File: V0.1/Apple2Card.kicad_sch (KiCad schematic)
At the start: 61 parts, among them J1 Conn_01x08_Pin, P2 Conn_02x13_Top_Bottom, Q1 BS170, SW1 SW_DIP_x08, U1C1 74LS240, U1E1 74LS14, U2 74LS133, U2B1 74LS08, U2D1 74LS138, U2E1 74LS08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

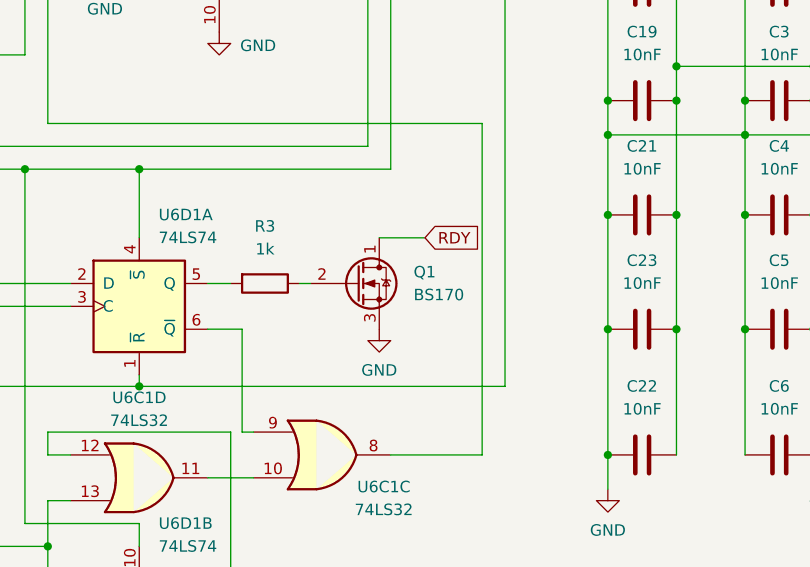
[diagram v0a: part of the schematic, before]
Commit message: BS170 to 2N3904
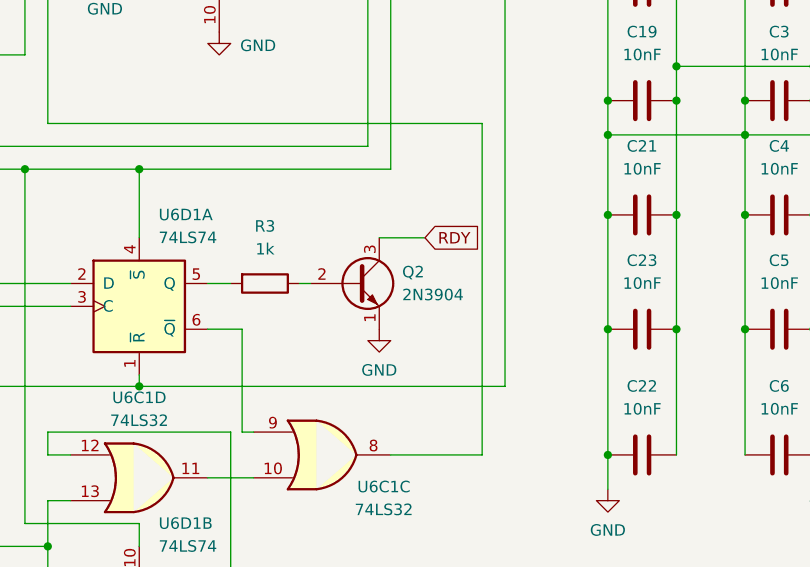
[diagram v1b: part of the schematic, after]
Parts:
- removed Q1: BS170, Package_TO_SOT_THT:TO-92_Inline, symbol Transistor_FET:BS170
- added Q2: 2N3904, Package_TO_SOT_THT:TO-92_Inline, symbol Transistor_BJT:2N3904
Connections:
- net GND: now also Q2.1 (E)
- net RDY: now also Q2.3 (C)
- net at R3.1: now also Q2.2 (B)
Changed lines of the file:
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@@
 	)
 	(symbol
-		(lib_id "Transistor_FET:BS170")
-		(at 335.28 160.02 0)
-		(unit 1)
-		(exclude_from_sim no)
-		(in_bom yes)
-		(on_board yes)
-		(dnp no)
-		(fields_autoplaced yes)
-		(property "Reference" "Q1"
-			(at 341.63 158.7499 0)
-			(effects
-				(font
-					(size 1.27 1.27)
-				)
-				(justify left)
-			)
-		)
-		(property "Value" "BS170"
-			(at 341.63 161.2899 0)
-			(effects
-				(font
-					(size 1.27 1.27)
-				)
-				(justify left)
-			)
-		)
-		(property "Footprint" "Package_TO_SOT_THT:TO-92_Inline"
-			(at 340.36 161.925 0)
-			(effects
-				(font
-					(size 1.27 1.27)
-					(italic yes)
-				)
-				(justify left)
-				(hide yes)
-			)
-		)
-		(property "Datasheet" "https://www.onsemi.com/pub/Collateral/BS170-D.PDF"
-			(at 340.36 163.83 0)
-			(effects
-				(font
-					(size 1.27 1.27)
-				)
-				(justify left)
-				(hide yes)
-			)
-		)
-		(property "Description" "0.5A Id, 60V Vds, N-Channel MOSFET, TO-92"
-			(at 335.28 160.02 0)
-			(effects
-				(font
-					(size 1.27 1.27)
-				)
-				(hide yes)
-			)
-		)
-		(pin "3"
-		)
-		(pin "2"
-		)
-		(pin "1"
-		)
-		(instances
-			(project ""
-				(path "/b60c50d1-225e-415c-8712-7acb5e3dc8ea"
-					(reference "Q1")
-					(unit 1)
-				)
-			)
-		)
-	)
-	(symbol
 		(lib_id "power:GND")
 		(at 300.99 73.66 0)
@@
 				)
 			)
+		)
+	)
+	(symbol
+		(lib_id "Transistor_BJT:2N3904")
+		(at 335.28 160.02 0)
+		(unit 1)
+		(exclude_from_sim no)
+		(in_bom yes)
+		(on_board yes)
+		(dnp no)
+		(fields_autoplaced yes)
+		(property "Reference" "Q2"
+			(at 340.36 158.7499 0)
+			(effects
+				(font
+					(size 1.27 1.27)
+				)
+				(justify left)
+			)
+		)
+		(property "Value" "2N3904"
+			(at 340.36 161.2899 0)
+			(effects
+				(font
+					(size 1.27 1.27)
+				)
+				(justify left)
+			)
+		)
+		(property "Footprint" "Package_TO_SOT_THT:TO-92_Inline"
+			(at 340.36 161.925 0)
+			(effects
+				(font
+					(size 1.27 1.27)
+					(italic yes)
+				)
+				(justify left)
+				(hide yes)
+			)
+		)
+		(property "Datasheet" "https://www.onsemi.com/pub/Collateral/2N3903-D.PDF"
+			(at 335.28 160.02 0)
+			(effects
+				(font
+					(size 1.27 1.27)
+				)
+				(justify left)
+				(hide yes)
+			)
+		)
+		(property "Description" "0.2A Ic, 40V Vce, Small Signal NPN Transistor, TO-92"
+			(at 335.28 160.02 0)
+			(effects
+				(font
+					(size 1.27 1.27)
+				)
+				(hide yes)
+			)
+		)
+		(property "Sim.Device" "NPN"
+			(at 335.28 160.02 0)
+			(effects
+				(font
+					(size 1.27 1.27)
+				)
+				(hide yes)
+			)
+		)
+		(property "Sim.Pins" "1=E 2=B 3=C"
+			(at 335.28 160.02 0)
+			(effects
+				(font
+					(size 1.27 1.27)
+				)
+				(hide yes)
+			)
+		)
+		(pin "3"
+		)
+		(pin "1"
+		)
+		(pin "2"
+		)
+		(instances
+			(project ""
+				(path "/b60c50d1-225e-415c-8712-7acb5e3dc8ea"
+					(reference "Q2")
+					(unit 1)
+				)
+			)
